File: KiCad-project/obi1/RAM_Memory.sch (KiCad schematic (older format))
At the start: 5 parts, among them IC1 RAM

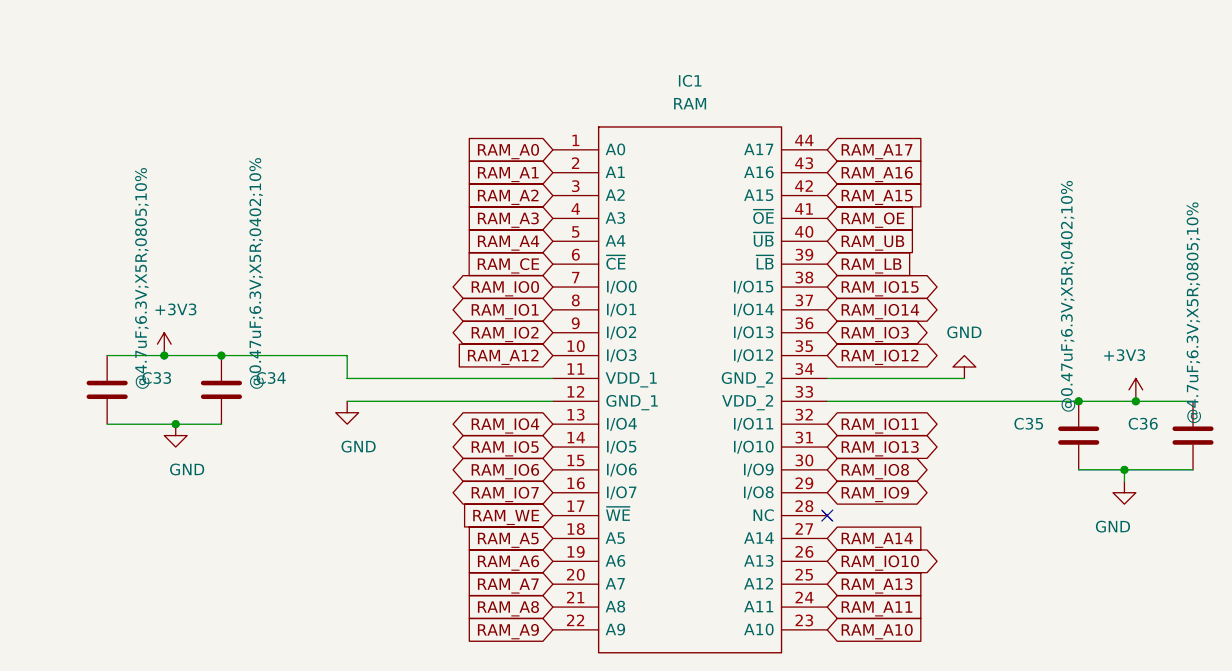
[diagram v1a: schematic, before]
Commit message: Changed RAM by Cypres Model -rebuild symbolic and changed footprint
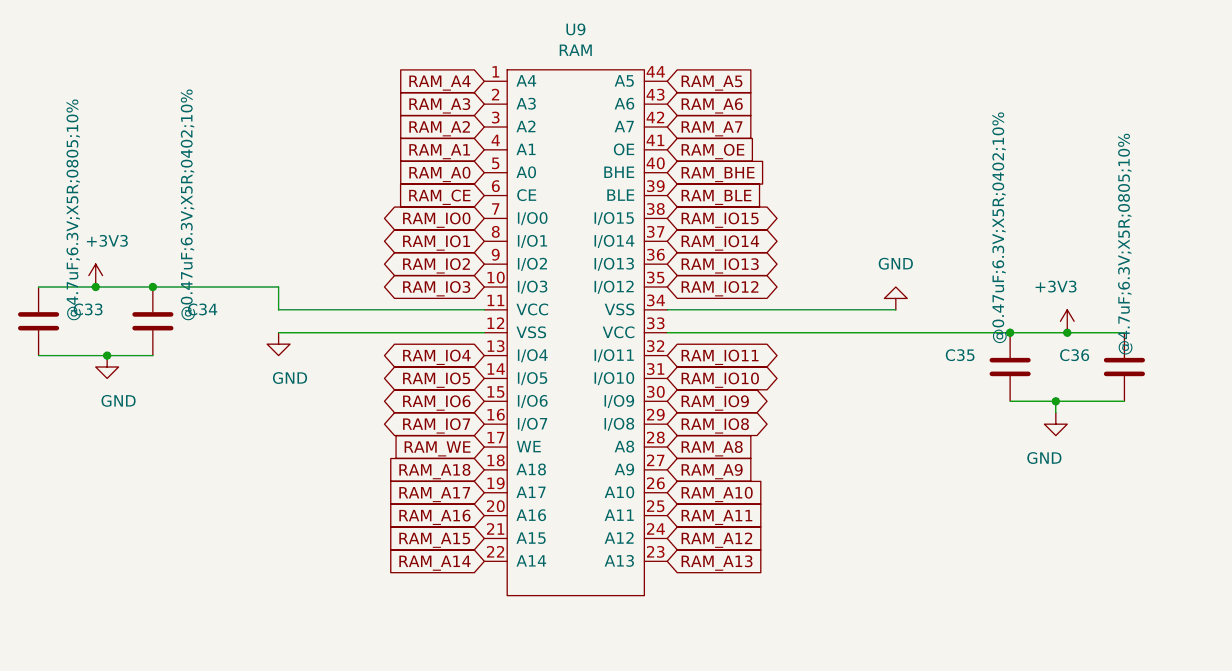
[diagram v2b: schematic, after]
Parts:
- removed IC1: RAM, egalan_lib:SOP80P1176X120-44N, symbol egalan:IS61WV25616EDBLL-10TLI
- added U9: RAM, egalan:SOP80P1176X120-44N, symbol egalan:CY62157eV30MoBL44TSOPII
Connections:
- net +3V3: now also U9.11 (VCC), U9.33 (VCC)
- net GND: now also U9.12 (VSS), U9.34 (VSS)
- net RAM_A0: now also U9.5 (A0)
- net RAM_A1: now also U9.4 (A1)
- net RAM_A10: now also U9.26 (A10)
- net RAM_A11: now also U9.25 (A11)
- net RAM_A12: now also U9.24 (A12)
- net RAM_A13: now also U9.23 (A13)
- net RAM_A14: now also U9.22 (A14)
- net RAM_A15: now also U9.21 (A15)
- net RAM_A16: now also U9.20 (A16)
- net RAM_A17: now also U9.19 (A17)
- net RAM_A2: now also U9.3 (A2)
- net RAM_A3: now also U9.2 (A3)
- net RAM_A4: now also U9.1 (A4)
- net RAM_A5: now also U9.44 (A5)
- net RAM_A6: now also U9.43 (A6)
- net RAM_A7: now also U9.42 (A7)
- net RAM_A8: now also U9.28 (A8)
- net RAM_A9: now also U9.27 (A9)
- net RAM_CE: now also U9.6 (CE)
- net RAM_IO0: now also U9.7 (I/O0)
- net RAM_IO1: now also U9.8 (I/O1)
- net RAM_IO10: now also U9.31 (I/O10)
- net RAM_IO11: now also U9.32 (I/O11)
- net RAM_IO12: now also U9.35 (I/O12)
- net RAM_IO13: now also U9.36 (I/O13)
- net RAM_IO14: now also U9.37 (I/O14)
- net RAM_IO15: now also U9.38 (I/O15)
- net RAM_IO2: now also U9.9 (I/O2)
- net RAM_IO3: now also U9.10 (I/O3)
- net RAM_IO4: now also U9.13 (I/O4)
- net RAM_IO5: now also U9.14 (I/O5)
- net RAM_IO6: now also U9.15 (I/O6)
- net RAM_IO7: now also U9.16 (I/O7)
- net RAM_IO8: now also U9.29 (I/O8)
- net RAM_IO9: now also U9.30 (I/O9)
- net RAM_OE: now also U9.41 (OE)
- net RAM_WE: now also U9.17 (WE)
- new net RAM_A18: U9.18 (A18)
- new net RAM_BHE: U9.40 (BHE)
- new net RAM_BLE: U9.39 (BLE)
- no-connect marks 1 -> 0
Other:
- moved on the sheet: C33, C34, C35, C36
